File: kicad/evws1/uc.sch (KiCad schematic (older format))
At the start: 62 parts, among them J13 atmega-isp-6, J14 header, M5 rpi-ev-plc-adapter-v1.0, Q3 AO3400, SW3 SW_Push, SW4 dip-switch-4x2pos-smd-1.27mm, SW5 SS-12D00G3, U1 atmega324p-20au, U4 PCF8591, U7 DS1307ZN, U8 24LC512, U9 PCF8574, Y1 20MHz, Y4 32768kHz

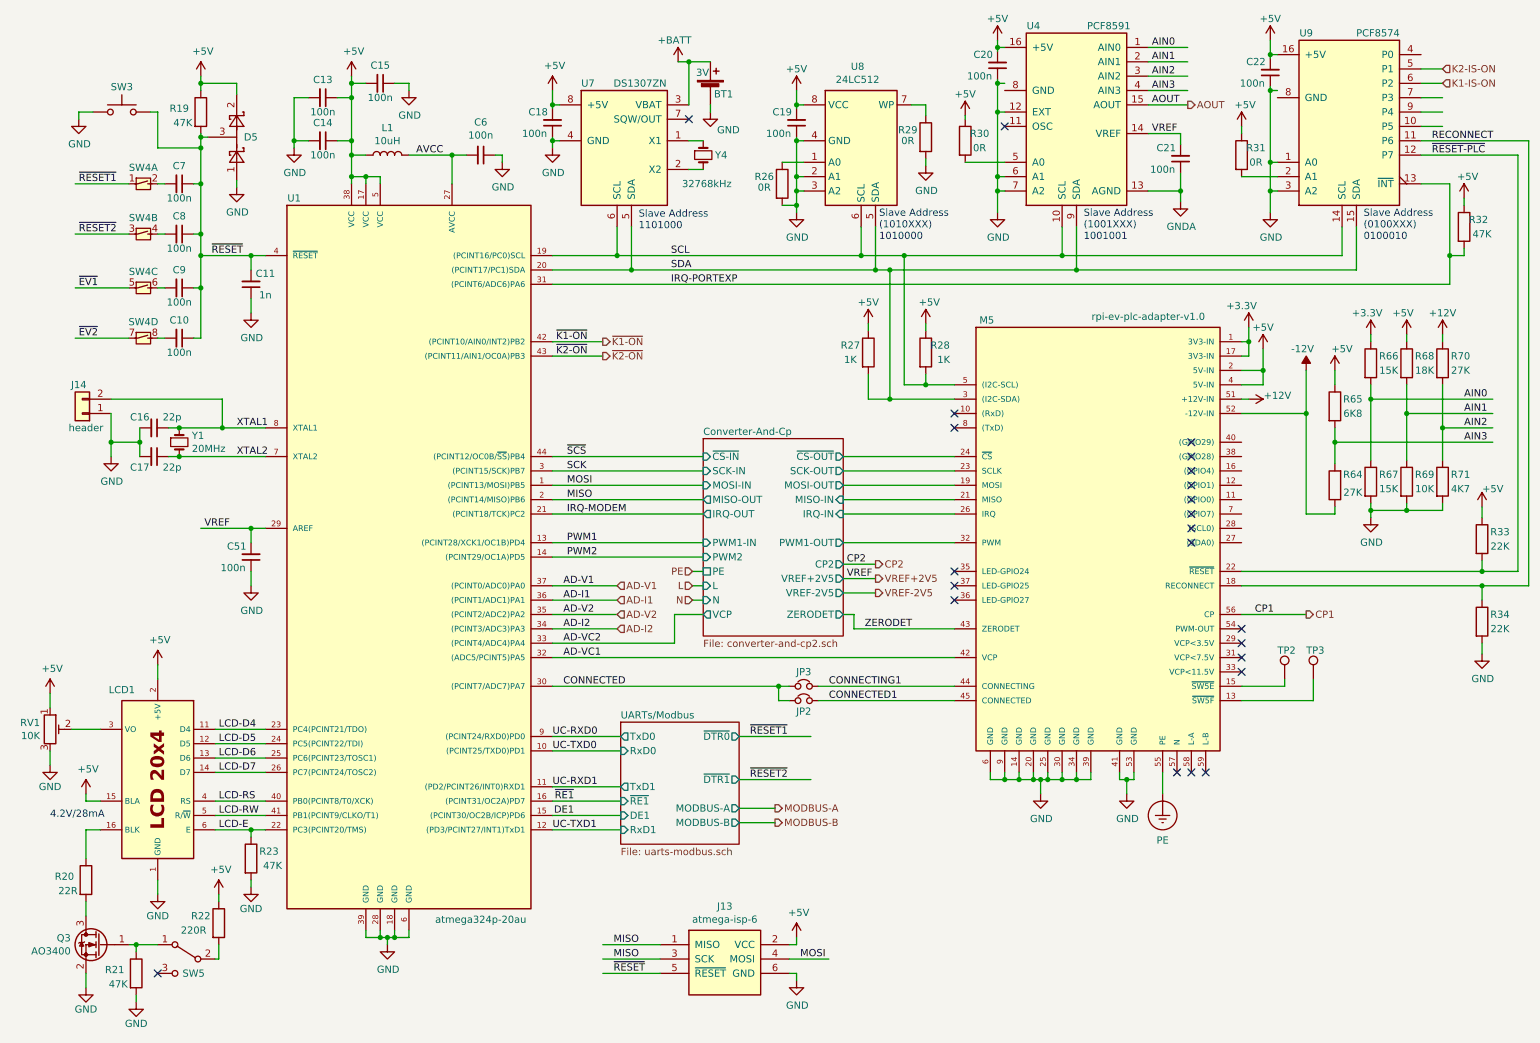
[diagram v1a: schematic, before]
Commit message: Schematic completed, no DRC errors left
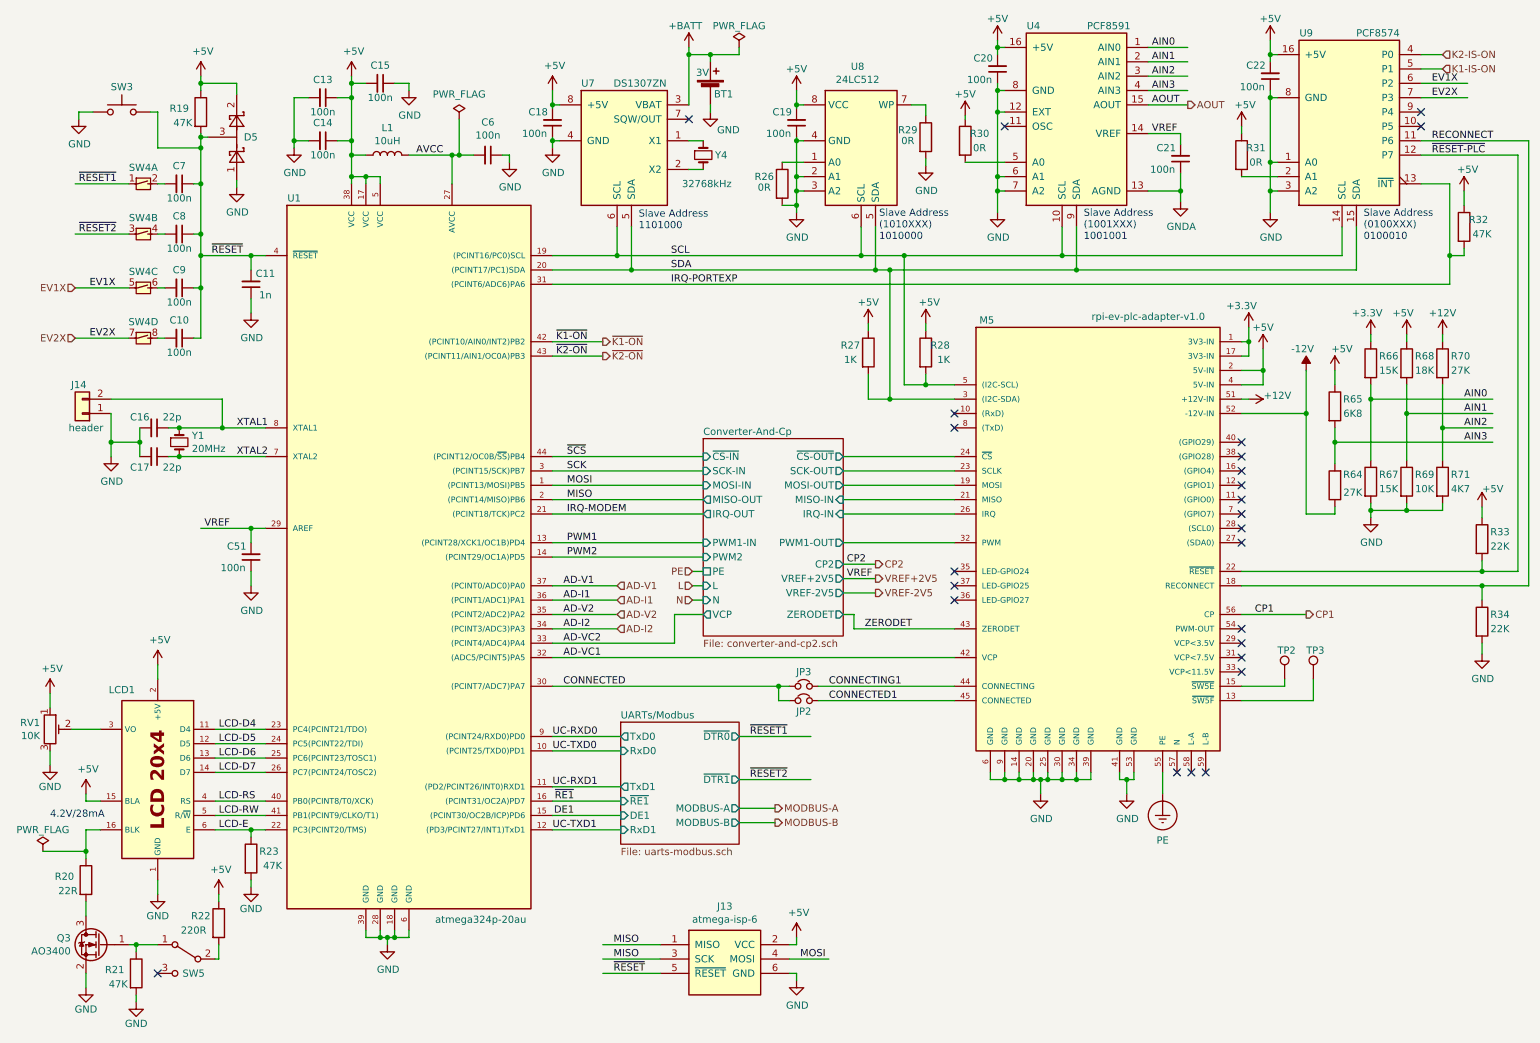
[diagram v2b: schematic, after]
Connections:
- net labels added: EV1X, EV2X
- net labels removed: ~EV1, ~EV2
- wire segments 348 -> 354
- no-connect marks 23 -> 25
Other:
- moved on the sheet: C20, C22, C6
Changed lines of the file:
@@
 L Device:C_Small C6
 U 1 1 5E1B0981
-P 3800 1550
-F 0 "C6" V 3571 1550 50  0000 C CNN
-F 1 "100n" V 3662 1550 50  0000 C CNN
-F 2 "Project:c-1206-hand-soldering" H 3800 1550 50  0001 C CNN
-F 3 "~" H 3800 1550 50  0001 C CNN
-	1    3800 1550
+P 3850 1550
+F 0 "C6" V 3621 1550 50  0000 C CNN
+F 1 "100n" V 3712 1550 50  0000 C CNN
+F 2 "Project:c-1206-hand-soldering" H 3850 1550 50  0001 C CNN
+F 3 "~" H 3850 1550 50  0001 C CNN
+	1    3850 1550
 	0    1    1    0
 $EndComp
@@
 L power:GND #PWR?
 U 1 1 5E1B0A92
-P 3950 1600
+P 4000 1600
 AR Path="/5E1B0A92" Ref="#PWR?"  Part="1"
 AR Path="/5E0A3961/5E1B0A92" Ref="#PWR0137"  Part="1"
-F 0 "#PWR0137" H 3950 1350 50  0001 C CNN
-F 1 "GND" H 3955 1427 50  0000 C CNN
-F 2 "" H 3950 1600 50  0001 C CNN
-F 3 "" H 3950 1600 50  0001 C CNN
-	1    3950 1600
-	1    0    0    -1
-$EndComp
-Wire Wire Line
-	3700 1550 3600 1550
+F 0 "#PWR0137" H 4000 1350 50  0001 C CNN
+F 1 "GND" H 4005 1427 50  0000 C CNN
+F 2 "" H 4000 1600 50  0001 C CNN
+F 3 "" H 4000 1600 50  0001 C CNN
+	1    4000 1600
+	1    0    0    -1
+$EndComp
 Connection ~ 3600 1550
 Wire Wire Line
-	3900 1550 3950 1550
-Wire Wire Line
-	3950 1550 3950 1600
+	3950 1550 4000 1550
+Wire Wire Line
+	4000 1550 4000 1600
 Wire Wire Line
 	2300 3450 2000 3450
@@
 Wire Wire Line
 	1350 2825 975  2825
-Text Label 1000 2475 0    50   ~ 0
-~EV1
-Text Label 1000 2825 0    50   ~ 0
-~EV2
 Connection ~ 1850 2100
 Wire Wire Line
@@
 Wire Wire Line
 	1050 6050 1150 6050
-Wire Wire Line
-	1150 6250 1050 6250
 $Comp
 L power:GND #PWR?
@@
 	1    0    0    -1
 $EndComp
-Wire Wire Line
-	1050 6450 1050 6250
 Wire Wire Line
 	1050 6750 1050 6850
@@
 Wire Wire Line
 	5400 1250 5400 1200
-Wire Wire Line
-	5400 900  5250 900
-Wire Wire Line
-	5250 900  5250 1200
 $Comp
 L power:+BATT #PWR?
 U 1 1 5E39A133
-P 5175 900
+P 5250 800
 AR Path="/5E39A133" Ref="#PWR?"  Part="1"
 AR Path="/5E0A3961/5E39A133" Ref="#PWR0106"  Part="1"
-F 0 "#PWR0106" H 5175 750 50  0001 C CNN
-F 1 "+BATT" H 5150 1050 50  0000 C CNN
-F 2 "" H 5175 900 50  0001 C CNN
-F 3 "" H 5175 900 50  0001 C CNN
-	1    5175 900
-	1    0    0    -1
-$EndComp
-Wire Wire Line
-	5250 900  5175 900
-Connection ~ 5250 900
+F 0 "#PWR0106" H 5250 650 50  0001 C CNN
+F 1 "+BATT" H 5225 950 50  0000 C CNN
+F 2 "" H 5250 800 50  0001 C CNN
+F 3 "" H 5250 800 50  0001 C CNN
+	1    5250 800
+	1    0    0    -1
+$EndComp
 NoConn ~ 5250 1300
 Wire Wire Line
@@
 L Device:C_Small C20
 U 1 1 5E59279C
-P 7400 925
-F 0 "C20" H 7500 850 50  0000 C CNN
-F 1 "100n" H 7525 1000 50  0000 C CNN
-F 2 "Project:c-1206-hand-soldering" H 7400 925 50  0001 C CNN
-F 3 "~" H 7400 925 50  0001 C CNN
-	1    7400 925
+P 7400 950
+F 0 "C20" H 7500 875 50  0000 C CNN
+F 1 "100n" H 7525 1025 50  0000 C CNN
+F 2 "Project:c-1206-hand-soldering" H 7400 950 50  0001 C CNN
+F 3 "~" H 7400 950 50  0001 C CNN
+	1    7400 950
 	-1   0    0    1
 $EndComp
@@
 Connection ~ 6550 2350
 NoConn ~ 7450 1350
-Wire Wire Line
-	7400 825  7400 800
-Wire Wire Line
-	7400 800  7450 800
-Wire Wire Line
-	7400 1025 7400 1050
 $Comp
 L power:GND #PWR?
@@
 Wire Wire Line
 	7450 1250 7400 1250
-Connection ~ 7400 1250
 Wire Wire Line
 	7400 1250 7400 1700
-$Comp
-L power:+5V #PWR?
-U 1 1 5E62D263
-P 7400 750
-AR Path="/5E62D263" Ref="#PWR?"  Part="1"
-AR Path="/5E0A3961/5E62D263" Ref="#PWR0158"  Part="1"
-F 0 "#PWR0158" H 7400 600 50  0001 C CNN
-F 1 "+5V" H 7400 900 50  0000 C CNN
-F 2 "" H 7400 750 50  0001 C CNN
-F 3 "" H 7400 750 50  0001 C CNN
-	1    7400 750
-	1    0    0    -1
-$EndComp
-Wire Wire Line
-	7400 800  7400 750
-Connection ~ 7400 800
 $Comp
 L power:+5V #PWR?
@@
 Wire Wire Line
 	6900 1575 6900 1625
-Wire Wire Line
-	7450 1050 7400 1050
-Connection ~ 7400 1050
-Wire Wire Line
-	7400 1050 7400 1250
 $Comp
 L Device:C_Small C21
@@
 L Device:C_Small C22
 U 1 1 5E95EBC4
-P 9300 975
-F 0 "C22" H 9400 900 50  0000 C CNN
-F 1 "100n" H 9425 1050 50  0000 C CNN
-F 2 "Project:c-1206-hand-soldering" H 9300 975 50  0001 C CNN
-F 3 "~" H 9300 975 50  0001 C CNN
-	1    9300 975
+P 9300 1000
+F 0 "C22" H 9400 925 50  0000 C CNN
+F 1 "100n" H 9425 1075 50  0000 C CNN
+F 2 "Project:c-1206-hand-soldering" H 9300 1000 50  0001 C CNN
+F 3 "~" H 9300 1000 50  0001 C CNN
+	1    9300 1000
 	-1   0    0    1
 $EndComp
@@
 	9350 1700 9100 1700
 Wire Wire Line
-	9300 1075 9300 1100
-Wire Wire Line
-	9350 1100 9300 1100
-Connection ~ 9300 1100
-Wire Wire Line
-	9300 1100 9300 1600
-Wire Wire Line
-	9350 850  9300 850
-Wire Wire Line
-	9300 850  9300 875
-Wire Wire Line
-	9300 850  9300 750
-Connection ~ 9300 850
-Wire Wire Line
 	9350 1600 9300 1600
-Connection ~ 9300 1600
 Wire Wire Line
 	9300 1600 9300 1800
@@
 	1    0    0    -1
 $EndComp
-Wire Wire Line
-	9100 1400 9100 1350
 Text HLabel 4650 2850 2    50   Output ~ 0
 ~K1-ON
@@
 L power:+5V #PWR?
 U 1 1 5EB7F783
-P 10650 1850
+P 10650 1800
 AR Path="/5EB7F783" Ref="#PWR?"  Part="1"
 AR Path="/5E0A3961/5EB7F783" Ref="#PWR0164"  Part="1"
-F 0 "#PWR0164" H 10650 1700 50  0001 C CNN
-F 1 "+5V" H 10675 2000 50  0000 C CNN
-F 2 "" H 10650 1850 50  0001 C CNN
-F 3 "" H 10650 1850 50  0001 C CNN
-	1    10650 1850
-	1    0    0    -1
-$EndComp
-Wire Wire Line
-	10650 1900 10650 1850
+F 0 "#PWR0164" H 10650 1650 50  0001 C CNN
+F 1 "+5V" H 10675 1950 50  0000 C CNN
+F 2 "" H 10650 1800 50  0001 C CNN
+F 3 "" H 10650 1800 50  0001 C CNN
+	1    10650 1800
+	1    0    0    -1
+$EndComp
 Wire Wire Line
 	10550 1750 10550 2250
@@
 Wire Wire Line
 	10550 2250 10550 2450
-Text HLabel 10500 1050 2    50   Input ~ 0
+Text HLabel 10500 950  2    50   Input ~ 0
 K1-IS-ON
-Text HLabel 10500 950  2    50   Input ~ 0
+Text HLabel 10500 850  2    50   Input ~ 0
 K2-IS-ON
 Wire Wire Line
 	10350 950  10500 950
-Wire Wire Line
-	10500 1050 10350 1050
-Wire Wire Line
-	10350 1150 10500 1150
-Wire Wire Line
-	10350 1250 10500 1250
-Wire Wire Line
-	10350 1350 10500 1350
 Wire Wire Line
 	10350 1550 11025 1550
@@
 NoConn ~ 7100 3350
 NoConn ~ 7100 3450
-NoConn ~ 8750 3550
-NoConn ~ 8750 3650
-NoConn ~ 8750 3750
-NoConn ~ 8750 3850
-NoConn ~ 8750 3950
-NoConn ~ 8750 4050
+NoConn ~ 9100 3550
+NoConn ~ 9100 3650
+NoConn ~ 9100 3750
+NoConn ~ 9100 3850
+NoConn ~ 9100 3950
+NoConn ~ 9100 4050
 NoConn ~ 9100 4950
 NoConn ~ 9100 5050
@@
 PE
 NoConn ~ 8650 5850
-NoConn ~ 8750 4150
-NoConn ~ 8750 4250
+NoConn ~ 9100 4150
+NoConn ~ 9100 4250
 $Comp
 L power:+12V #PWR?
@@
 Connection ~ 9150 2850
 Wire Wire Line
-	9100 3050 9250 3050
-Wire Wire Line
-	9250 3050 9250 2900
-Wire Wire Line
-	9100 3150 9250 3150
-Wire Wire Line
-	9250 3150 9250 3050
-Connection ~ 9250 3050
-Wire Wire Line
 	9100 3250 9150 3250
 Wire Wire Line
@@
 	1    0    0    -1
 $EndComp
+Wire Wire Line
+	9250 2900 9250 3050
+Wire Wire Line
+	9250 3150 9100 3150
+Wire Wire Line
+	9250 3050 9100 3050
+Connection ~ 9250 3050
+Wire Wire Line
+	9250 3050 9250 3150
+NoConn ~ 10350 1250
+Wire Wire Line
+	1050 6450 1050 6400
+Wire Wire Line
+	1050 6250 1150 6250
+$Comp
+L power:+5V #PWR?
+U 1 1 5E62D263
+P 7400 750
+AR Path="/5E62D263" Ref="#PWR?"  Part="1"
+AR Path="/5E0A3961/5E62D263" Ref="#PWR0158"  Part="1"
+F 0 "#PWR0158" H 7400 600 50  0001 C CNN
+F 1 "+5V" H 7400 900 50  0000 C CNN
+F 2 "" H 7400 750 50  0001 C CNN
+F 3 "" H 7400 750 50  0001 C CNN
+	1    7400 750
+	1    0    0    -1
+$EndComp
+Wire Wire Line
+	7450 800  7400 800
+Wire Wire Line
+	7400 800  7400 750
+Wire Wire Line
+	7400 800  7400 850
+Connection ~ 7400 800
+Wire Wire Line
+	7400 1050 7400 1100
+Wire Wire Line
+	7400 1100 7450 1100
+Wire Wire Line
+	7400 1250 7400 1100
+Connection ~ 7400 1250
+Connection ~ 7400 1100
+Wire Wire Line
+	9350 850  9300 850
+Wire Wire Line
+	9300 850  9300 900
+Wire Wire Line
+	9300 850  9300 750
+Connection ~ 9300 850
+Wire Wire Line
+	9300 1600 9300 1150
+Connection ~ 9300 1600
+Wire Wire Line
+	9350 1150 9300 1150
+Connection ~ 9300 1150
+Wire Wire Line
+	9300 1150 9300 1100
+Wire Wire Line
+	9100 1400 9100 1350
+Wire Wire Line
+	10650 1900 10650 1800
+$Comp
+L power:PWR_FLAG #FLG?
+U 1 1 5E6B24A3
+P 5600 800
+AR Path="/5E6B24A3" Ref="#FLG?"  Part="1"
+AR Path="/5E0A3961/5E6B24A3" Ref="#FLG0105"  Part="1"
+F 0 "#FLG0105" H 5600 875 50  0001 C CNN
+F 1 "PWR_FLAG" H 5600 950 50  0000 C CNN
+F 2 "" H 5600 800 50  0001 C CNN
+F 3 "~" H 5600 800 50  0001 C CNN
+	1    5600 800
+	1    0    0    -1
+$EndComp
+Wire Wire Line
+	5250 1200 5250 850
+Wire Wire Line
+	5250 850  5400 850
+Wire Wire Line
+	5400 850  5400 900
+Connection ~ 5250 850
+Wire Wire Line
+	5250 850  5250 800
+Wire Wire Line
+	5400 850  5600 850
+Wire Wire Line
+	5600 850  5600 800
+Connection ~ 5400 850
+$Comp
+L power:PWR_FLAG #FLG?
+U 1 1 5E728967
+P 750 6400
+AR Path="/5E728967" Ref="#FLG?"  Part="1"
+AR Path="/5E0A3961/5E728967" Ref="#FLG0106"  Part="1"
+F 0 "#FLG0106" H 750 6475 50  0001 C CNN
+F 1 "PWR_FLAG" H 750 6550 50  0000 C CNN
+F 2 "" H 750 6400 50  0001 C CNN
+F 3 "~" H 750 6400 50  0001 C CNN
+	1    750  6400
+	1    0    0    -1
+$EndComp
+Wire Wire Line
+	750  6400 1050 6400
+Connection ~ 1050 6400
+Wire Wire Line
+	1050 6400 1050 6250
+Text HLabel 975  2475 0    50   Input ~ 0
+EV1X
+Text HLabel 975  2825 0    50   Input ~ 0
+EV2X
+Text Label 1075 2475 0    50   ~ 0
+EV1X
+Text Label 1075 2825 0    50   ~ 0
+EV2X
+Wire Wire Line
+	10350 1050 10675 1050
+NoConn ~ 10350 1350
+Wire Wire Line
+	10500 850  10350 850
+Text Label 10425 1050 0    50   ~ 0
+EV1X
+Wire Wire Line
+	10350 1150 10675 1150
+Text Label 10425 1150 0    50   ~ 0
+EV2X
+$Comp
+L power:PWR_FLAG #FLG?
+U 1 1 5EAC6A3D
+P 3650 1300
+AR Path="/5EAC6A3D" Ref="#FLG?"  Part="1"
+AR Path="/5E0A3961/5EAC6A3D" Ref="#FLG0107"  Part="1"
+F 0 "#FLG0107" H 3650 1375 50  0001 C CNN
+F 1 "PWR_FLAG" H 3650 1474 50  0000 C CNN
+F 2 "" H 3650 1300 50  0001 C CNN
+F 3 "~" H 3650 1300 50  0001 C CNN
+	1    3650 1300
+	1    0    0    -1
+$EndComp
+Wire Wire Line
+	3600 1550 3650 1550
+Wire Wire Line
+	3650 1300 3650 1550
+Connection ~ 3650 1550
+Wire Wire Line
+	3650 1550 3750 1550
 $EndSCHEMATC
